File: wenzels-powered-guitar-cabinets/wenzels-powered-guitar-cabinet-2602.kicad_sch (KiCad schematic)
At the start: 36 parts, among them J1 AC power in, J10 IN 2, J2 Discrete Class AB MOSFET ampl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, J3 Speaker 2, J4 Switching-Mode Power Supply, J5 Discrete Class AB MOSFET ampl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, J6 Discrete Class AB MOSFET ampl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, J7 Discrete Class AB MOSFET ampl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, J8 IN 1, J9 Speaker 1, M1 12V Noctua NF-A9 PWM 92mm, T1 TY250P, T2 TY250P

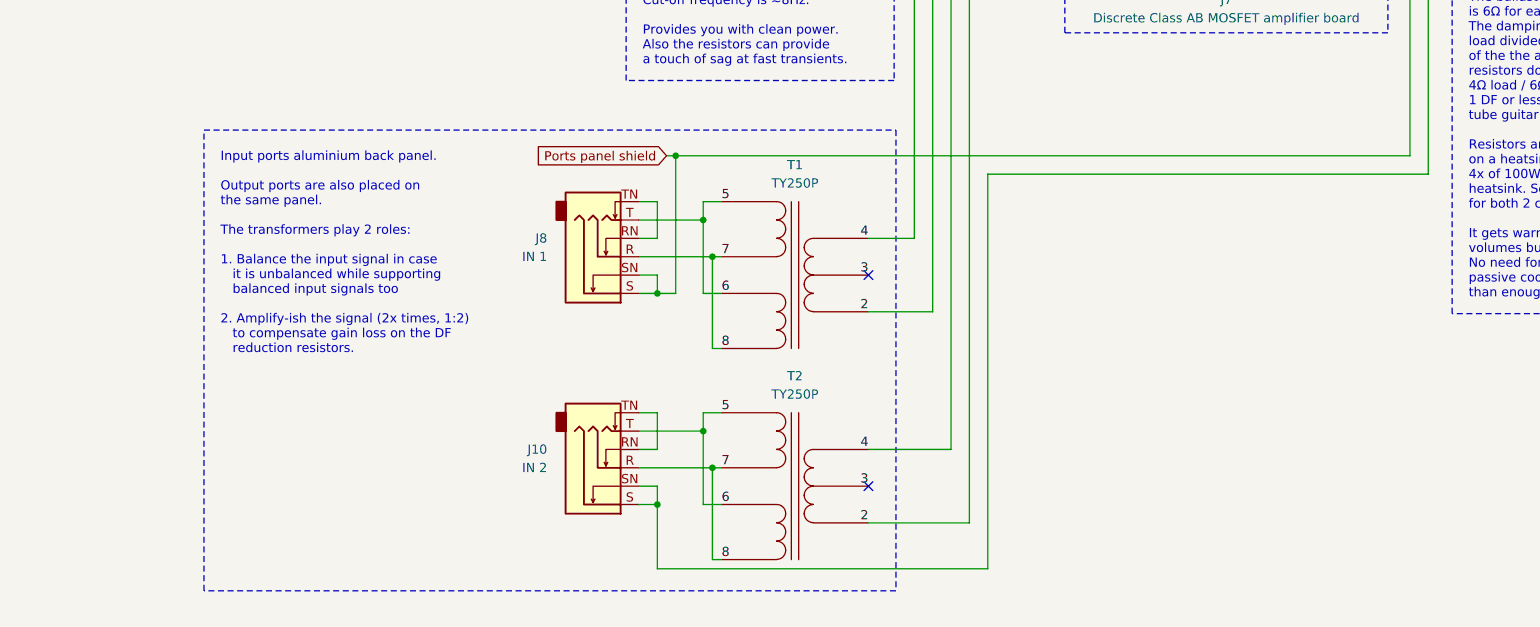
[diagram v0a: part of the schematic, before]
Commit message: wenzels-powered-guitar-cabinet-2602: release r1-wip-2 (WIP/prototyping)
Add LEVEL switches for the input transformers and GND LIFT switches for
the input ports.
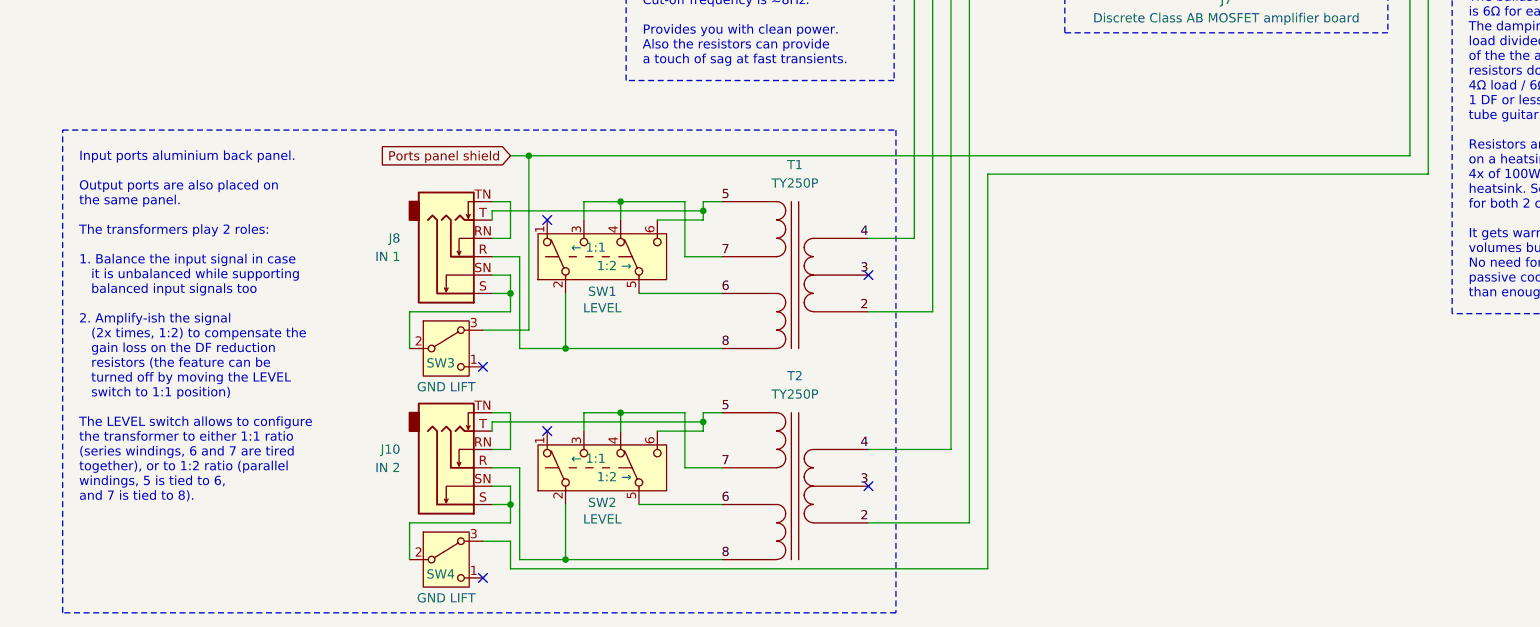
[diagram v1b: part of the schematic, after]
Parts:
- added SW1, SW2: LEVEL, symbol Switch:SW_Push_DPDT
- added SW3, SW4: GND LIFT, Button_Switch_SMD:Nidec_Copal_CAS-120A, symbol Switch:SW_Nidec_CAS-120A1
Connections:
- net 5: now also SW1.6 (C), SW2.6 (C); no longer T1.6 (OUT2A), T2.6 (OUT2A)
- net 7: now also SW1.3 (C), SW1.4 (A), SW2.3 (C), SW2.4 (A); no longer J10.R, J8.R, T1.7 (OUT2B), T2.7 (OUT2B)
- net Ports panel shield: now also SW3.3 (A), SW4.3 (A); no longer J10.S, J10.SN, J8.S, J8.SN
- new net: J10.S, J10.SN, SW4.2 (B)
- new net: J8.S, J8.SN, SW3.2 (B)
- new net 6: SW1.5 (B), SW2.5 (B), T1.6 (OUT2A), T2.6 (OUT2A)
- new net 8: J10.R, J8.R, SW1.2 (B), SW2.2 (B), T1.7 (OUT2B), T2.7 (OUT2B)
- no-connect marks 4 -> 8
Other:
- note added: "Input ports aluminium back panel. Output ports are also placed on the same panel. The transformers play 2 roles: 1. Balance the input signal in case it is unbalanced while supporting balanced input signals too 2. Amplify-ish the signal (2x times, 1:2) to compensate the gain loss on the DF reduction resistors (the feature can be turned off by moving the LEVEL switch to 1:1 position) The LEVEL swit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"
- note removed: "Input ports aluminium back panel. Output ports are also placed on the same panel. The transformers play 2 roles: 1. Balance the input signal in case it is unbalanced while supporting balanced input signals too 2. Amplify-ish the signal (2x times, 1:2) to compensate gain loss on the DF reduction resistors."
- moved on the sheet: J10

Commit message: wenzels-powered-guitar-cabinets: release-2602-cabinet-2026-03-r1
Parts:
- removed SW3, SW4: GND LIFT, Button_Switch_SMD:Nidec_Copal_CAS-120A, symbol Switch:SW_Nidec_CAS-120A1
- added HS3: Amp 1, symbol Mechanical:Heatsink_Pad
- added HS4: Amp 2, symbol Mechanical:Heatsink_Pad
- added M2: 12V Noctua NF-A12x25 PWM 120mm, symbol Motor:Fan
- added R1, R6: 10, symbol Device:R
- added SW3: GND-1, symbol Switch:SW_SPDT_MSM
- added SW4: GND-2, symbol Switch:SW_SPDT_MSM
- added SW5: PHASE, symbol Switch:SW_Push_DPDT
- J2, J5, J6, J7: Field5 (none) -> LJM L7 design
- M1: value 12V Noctua NF-A9 PWM 92mm -> 12V Noctua NF-A12x25 PWM 120mm
- renumbered HS2 to HS1, HS3 to HS2
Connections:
- net Common is gone; now on net Ports panel shield: C1.2, C2.1, C3.2, C4.1, HS1.1, HS2.1, J1.3 (PE), J2.2 (Pin_2), J4.2 (Pin_2), J4.5 (Pin_5), J4.SH (Shield), J5.5 (Pin_5), J6.2 (Pin_2), J7.5 (Pin_5)
- net Ports panel shield: now also HS3.1, HS4.1; no longer J2.5 (Pin_5), J5.2 (Pin_2), J6.5 (Pin_5), J7.2 (Pin_2)
- net at M1.1 (+), PS1.2 (Vout+): now also M2.1 (+)
- net at M1.2 (-), PS1.1 (Vout-): now also M2.2 (-)
- net at J10.S, J10.SN: now also SW4.2 (3)
- net at J8.S, J8.SN: now also SW3.2 (3)
- new net  R-Lifted: R1.2, R6.1, SW3.1, SW4.1
- new net Box shield: J2.5 (Pin_5), J5.2 (Pin_2), J6.5 (Pin_5), J7.2 (Pin_2), R1.1, R6.2, SW3.3 (4), SW4.3 (4)
- new net Ring: SW5.5 (B)
- new net TY250P pin 5: SW5.1 (A), SW5.6 (C)
- new net TY250P pin 8: SW5.3 (C), SW5.4 (A)
- new net Tip: SW5.2 (B)
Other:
- note added: "Phase-flip per-channel switch. Optional. I personally didn’t need it for my build (I have this option on my pedalboard). But it’s very easy to add since there is an input transformer."
- note added: "The input transformers (T1 and T2) play 2 roles: 1. Balance the input signal in case it is unbalanced while supporting balanced input signals too 2. Amplify-ish the signal (2x times, 1:2) to compensate the gain loss on the DF reduction resistors (the feature can be turned off by moving the LEVEL switch to 1:1 position) The LEVEL switch allows to configure the transformer to either 1:1 ratio (seri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"
- note removed: "Input ports aluminium back panel. Output ports are also placed on the same panel. The transformers play 2 roles: 1. Balance the input signal in case it is unbalanced while supporting balanced input signals too 2. Amplify-ish the signal (2x times, 1:2) to compensate the gain loss on the DF reduction resistors (the feature can be turned off by moving the LEVEL switch to 1:1 position) The LEVEL swit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"
- moved on the sheet: C1, C2, C29, C3, C30, C31, C32, C4, C65, C66, C67, C68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

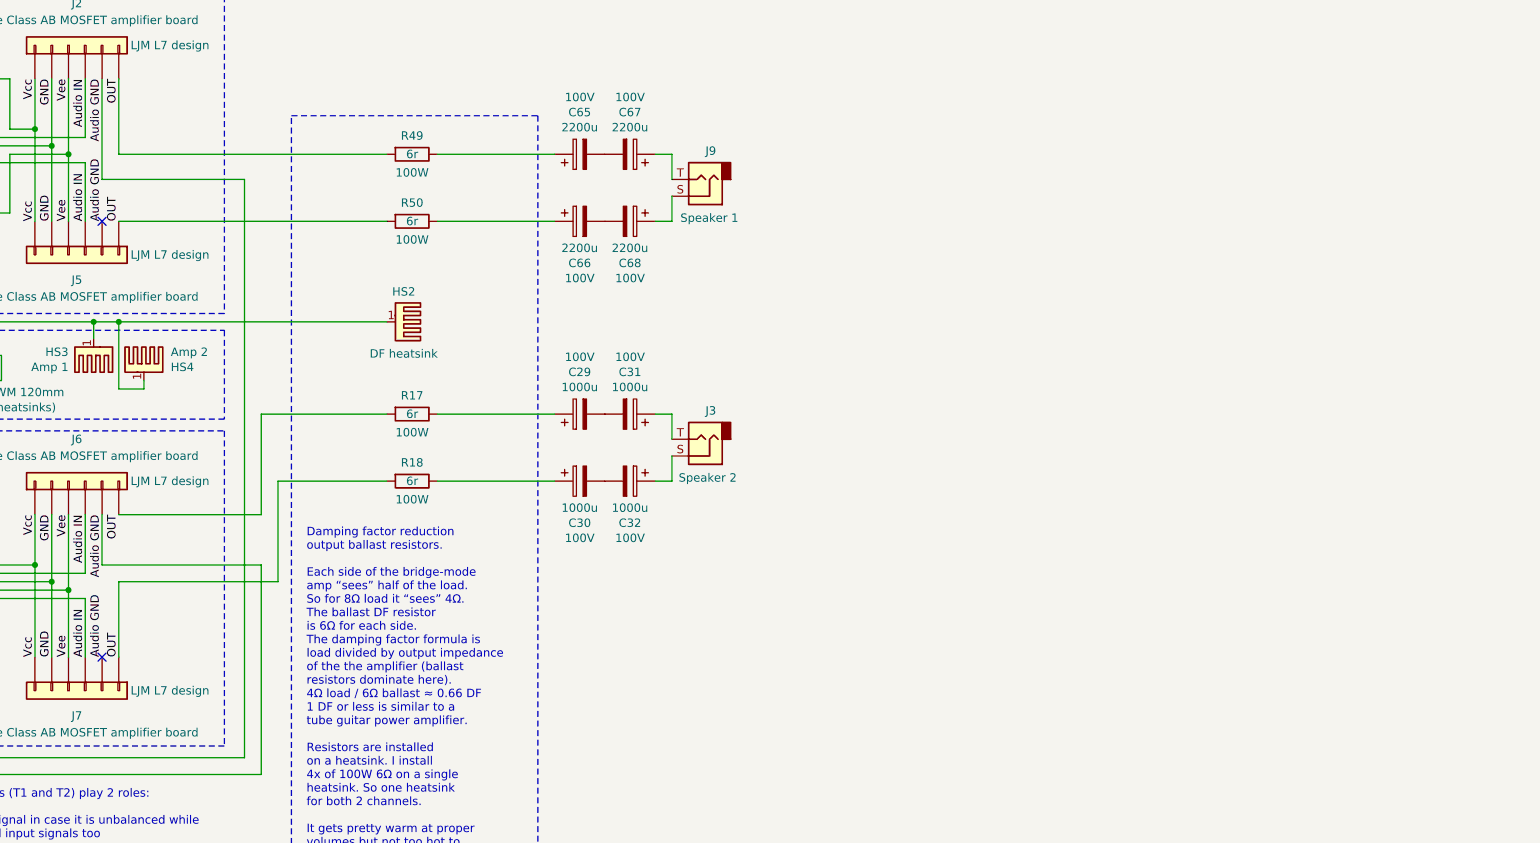
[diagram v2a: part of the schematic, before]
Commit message: wenzels-powered-guitar-cabinets 2601-r3 & 2602-r2 releases
Added impedance transformers and bleeder resistors for the output
capacitors.
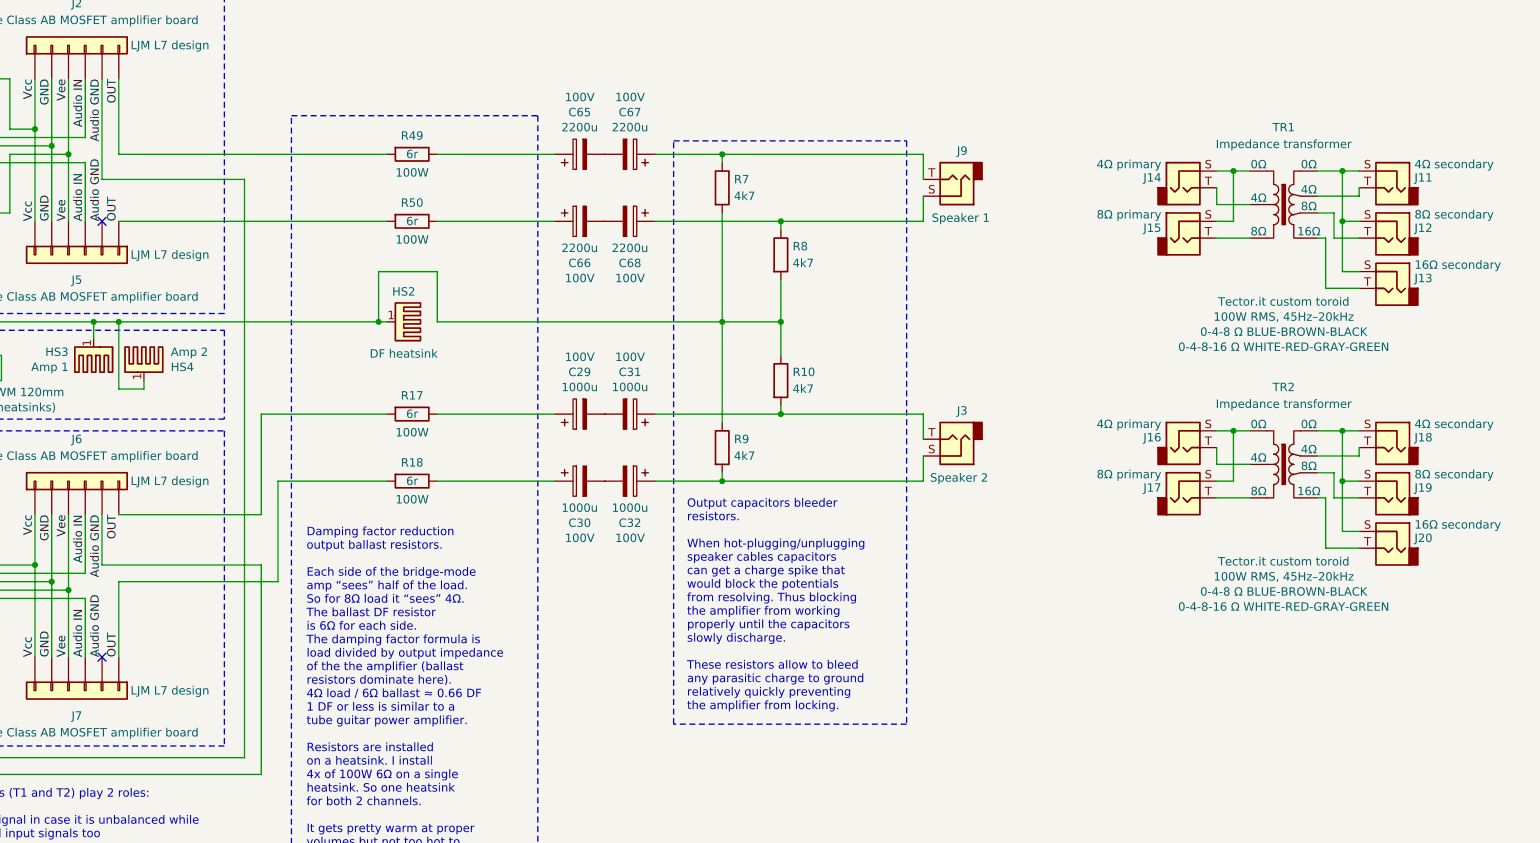
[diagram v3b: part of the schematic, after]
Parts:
- added J11, J18: 4Ω secondary, symbol Connector_Audio:AudioJack2
- added J12, J19: 8Ω secondary, symbol Connector_Audio:AudioJack2
- added J13, J20: 16Ω secondary, symbol Connector_Audio:AudioJack2
- added J14, J16: 4Ω primary, symbol Connector_Audio:AudioJack2
- added J15, J17: 8Ω primary, symbol Connector_Audio:AudioJack2
- added R10, R7, R8, R9: 4k7, symbol Device:R
- added TR1, TR2: Impedance transformer, symbol Transformer:TRANSF4
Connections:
- net Ports panel shield: now also R10.1, R7.2, R8.2, R9.1
- net at C67.1, J9.T: now also R7.1
- net at C32.1, J3.S: now also R9.2
- net at C31.1, J3.T: now also R10.2
- net at C68.1, J9.S: now also R8.1
- new net: J16.S, J17.S, TR2.1 (0Ω)
- new net: J17.T, TR2.3 (8Ω)
- new net: J14.S, J15.S, TR1.1 (0Ω)
- new net: J15.T, TR1.3 (8Ω)
- new net: J18.S, J19.S, J20.S, TR2.4 (0Ω)
- new net: J18.T, TR2.5 (4Ω)
- new net: J11.S, J12.S, J13.S, TR1.4 (0Ω)
- new net: J11.T, TR1.5 (4Ω)
- new net: J14.T, TR1.2 (4Ω)
- new net: J12.T, TR1.6 (8Ω)
- new net: J13.T, TR1.7 (16Ω)
- new net: J20.T, TR2.7 (16Ω)
- new net: J16.T, TR2.2 (4Ω)
- new net: J19.T, TR2.6 (8Ω)
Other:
- note added: "Output capacitors bleeder resistors. When hot-plugging/unplugging speaker cables capacitors can get a charge spike that would block the potentials from resolving. Thus blocking the amplifier from working properly until the capacitors slowly discharge. These resistors allow to bleed any parasitic charge to ground relatively quickly preventing the amplifier from locking."
- moved on the sheet: J3, J9
